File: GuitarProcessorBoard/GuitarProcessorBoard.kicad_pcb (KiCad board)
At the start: 4 copper layers, 86 x 65 mm, 123 parts, among them J301 SWD Header, J302 PWR, J304 MODE, J305 BYP, J307 ScopeGroundLoop, SW301 RST, SW302 BOOT, U201 TLV320AIC3204, U202 TL074, U301 STM32H7B0VBT6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

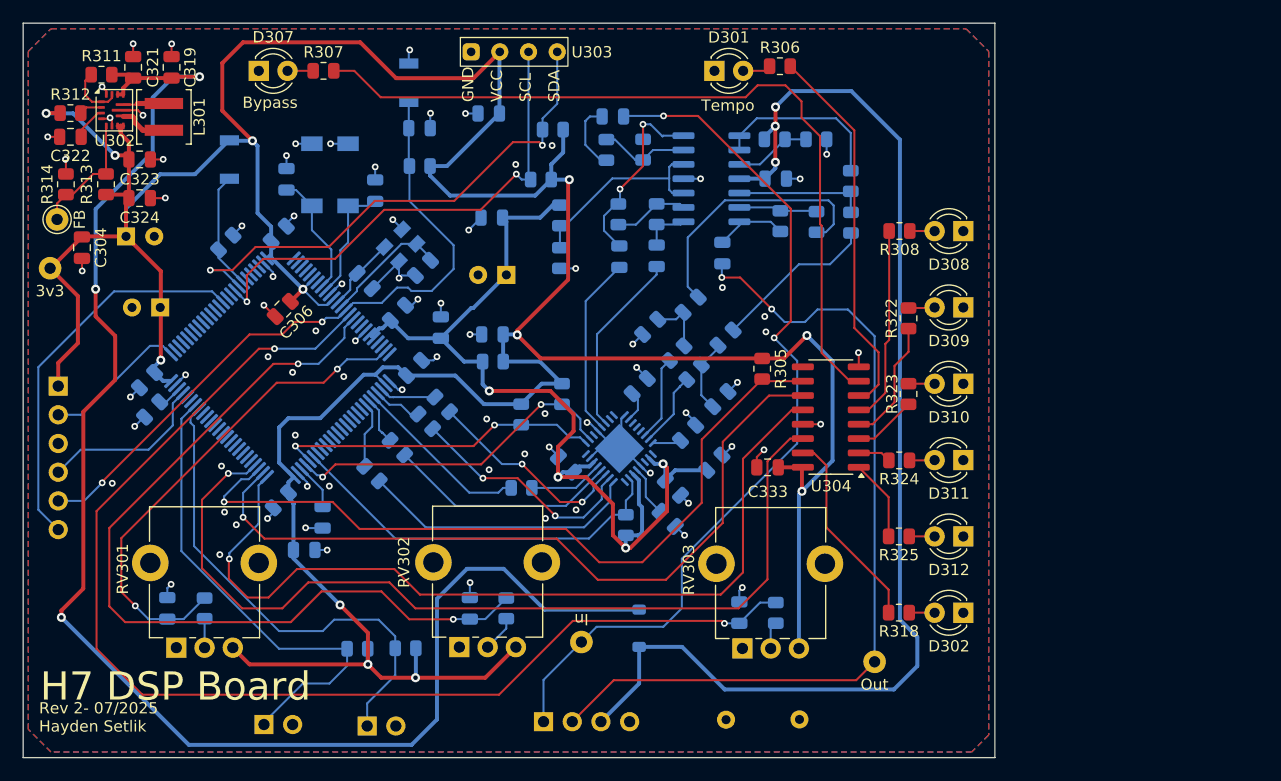
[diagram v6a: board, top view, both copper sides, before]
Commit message: split PSU schematic, DRC passing
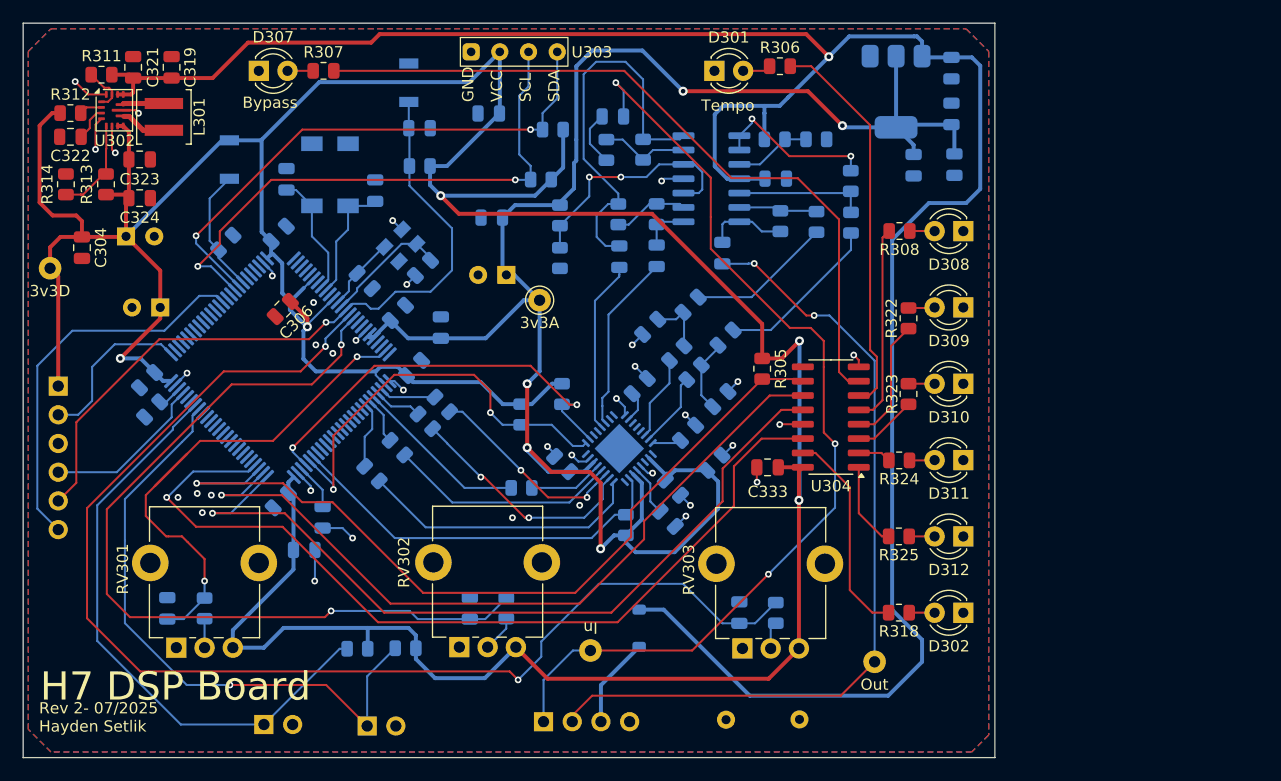
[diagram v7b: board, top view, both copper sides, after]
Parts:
- removed C316: 2u2, Capacitor_SMD:C_0805_2012Metric
- removed FB301: 90R, Resistor_SMD:R_0805_2012Metric
- removed TP305: FB, TestPoint:TestPoint_THTPad_D2.0mm_Drill1.0mm_VAL
- added C4: 100n, Capacitor_SMD:C_0805_2012Metric, B.Cu at (-96.8, 35.0)
- added C5: 100n, Capacitor_SMD:C_0805_2012Metric, B.Cu at (-96.8, 39.0)
- added C6: 1u, Capacitor_SMD:C_0805_2012Metric, B.Cu at (-100.2, 43.5)
- added C7: 10u, Capacitor_SMD:C_0805_2012Metric, B.Cu at (-96.5, 43.5)
- added TP1: 3v3A, TestPoint:TestPoint_THTPad_D2.0mm_Drill1.0mm_VAL, F.Cu at (-133.2, 55.5)
- added U1: AMS1117, Package_TO_SOT_SMD:SOT-223-3_TabPin2, B.Cu at (-101.7, 37.0)
- TP303: value 3v3 -> 3v3D
- moved TP301 1.10 mm to (-128.8, 86.5)
- moved C202 0.34 mm to (-131.2, 70.0)
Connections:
- C216 pad 1: +9V -> VCC
- R209 pad 1: +9V -> VCC
- U202 pad 4: +9V -> VCC
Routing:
- net +9V: track 106.2 -> 8.02 mm, vias 3 -> 0
- net +3.3VA: track 87.1 -> 158.8 mm, vias 4 -> 5
- net VCC: track 136.0 -> 197.9 mm, vias 3 -> 1
- net GND: track 92.0 -> 48.2 mm, vias 80 -> 37
- net /Audio/InputPos: track 18.3 -> 34.7 mm, vias 2 -> 0
- net BYP_BTN: track 43.5 -> 54.8 mm, vias 0 -> 1
- net Net-(C214-Pad2): track 23.6 -> 12.8 mm
- net MODE_BTN: track 42.8 -> 52.4 mm
- net FX_IN: track 77.8 -> 85.8 mm, vias 2 -> 3
- net CODEC_SCL: track 29.0 -> 36.6 mm
- net CODEC_SDA: track 30.1 -> 37.0 mm
- net +3.3V: track 339.0 -> 345.6 mm, vias 12 -> 5
- net ADC_A: track 44.2 -> 50.8 mm
- net LED_LATCH: track 76.5 -> 71.2 mm
- net DISP_SCL: track 44.2 -> 49.6 mm
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
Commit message: stitching vias, prettier layout
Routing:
- net GND: track 48.2 -> 95.6 mm, vias 37 -> 92
- net ADC_A: track 50.8 -> 42.7 mm
- net +3.3V: track 345.6 -> 353.2 mm
- net /MCU/LED_BYPASS: track 65.7 -> 62.3 mm
- net +3.3VA: track 158.8 -> 161.5 mm
- net CODEC_SCL: track 36.6 -> 35.1 mm
- net ADC_C: track 110.2 -> 109.1 mm
- net NRST: track 63.3 -> 64.4 mm
- net VCC: track 197.9 -> 196.9 mm
- net /Audio/Bias1: track 21.4 -> 20.9 mm
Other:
- board text added: "Rev 2- 01/2026 Hayden Setlik"
- board text removed: "Rev 2- 07/2025 Hayden Setlik"
